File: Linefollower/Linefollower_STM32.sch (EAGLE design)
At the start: 63 parts, among them IC2 L298, IC4 STM32F101RET6, Q1 CSM-7X-DU

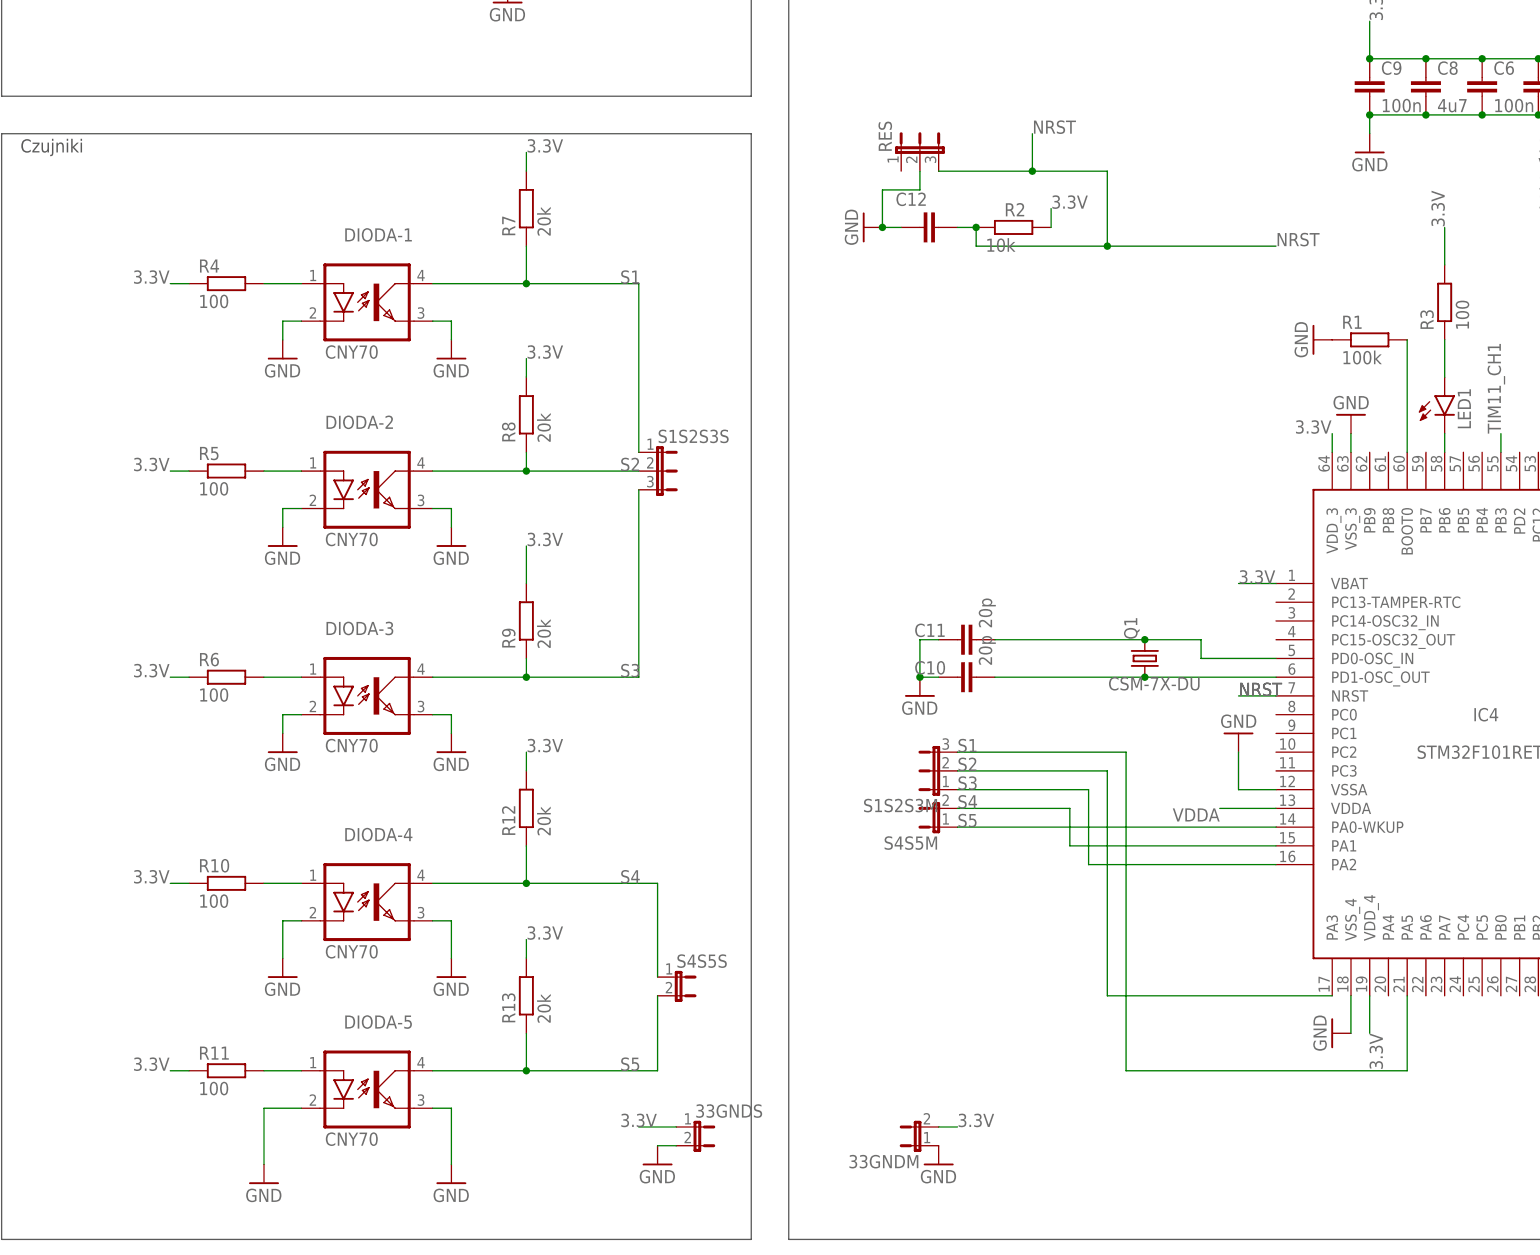
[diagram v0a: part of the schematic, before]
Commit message: 6 sensor strip
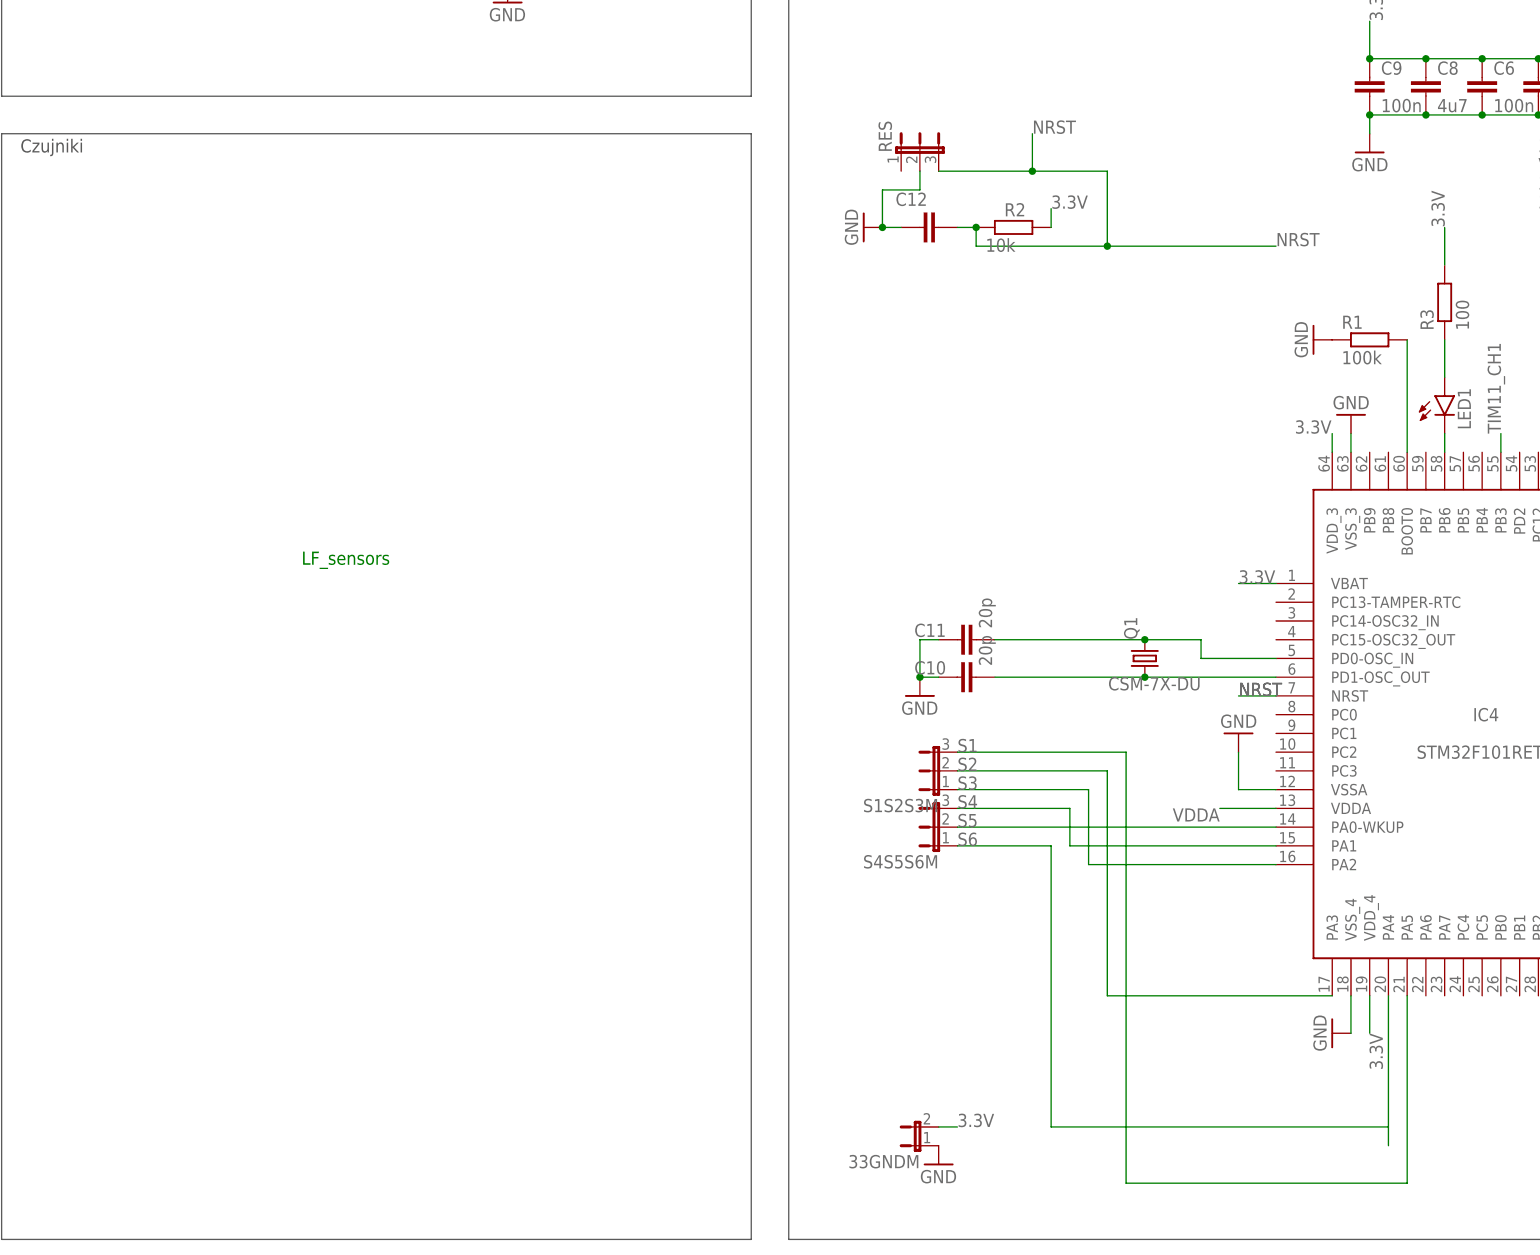
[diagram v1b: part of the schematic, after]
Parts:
- removed 33GNDS, S4S5M, S4S5S: (no value), jumper:JP1E
- removed DIODA-1, DIODA-2, DIODA-3, DIODA-4, DIODA-5: CNY70, optocoupler:LTV816
- removed R10, R11, R4, R5, R6: 100, rcl:R-EU_R0805
- removed R12, R13, R7, R8, R9: 20k, rcl:R-EU_R0805
- removed S1S2S3S: (no value), jumper:JP2E
- added S4S5S6M: (no value), jumper:JP2E
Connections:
- removed net N$10: DIODA-3.A, R6.2
- removed net N$11: DIODA-4.A, R10.2
- removed net N$14: DIODA-5.A, R11.2
- removed net N$8: DIODA-1.A, R4.2
- removed net N$9: DIODA-2.A, R5.2
- new net S6: IC4.PA4, S4S5S6M.1
- net 3.3V: no longer 33GNDS.1, R10.1, R11.1, R12.2, R13.2, R4.1, R5.1, R6.1, R7.2, R8.2, R9.2
- net GND: no longer 33GNDS.2, DIODA-1.C, DIODA-1.EMIT, DIODA-2.C, DIODA-2.EMIT, DIODA-3.C, DIODA-3.EMIT, DIODA-4.C, DIODA-4.EMIT, DIODA-5.C, DIODA-5.EMIT
- net S1: no longer DIODA-1.COL, R7.1, S1S2S3S.1
- net S2: no longer DIODA-2.COL, R8.1, S1S2S3S.2
- net S3: no longer DIODA-3.COL, R9.1, S1S2S3S.3
- net S4: now also S4S5S6M.3; no longer DIODA-4.COL, R12.1, S4S5M.2, S4S5S.1
- net S5: now also S4S5S6M.2; no longer DIODA-5.COL, R13.1, S4S5M.1, S4S5S.2
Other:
- note added: "LF_sensors"
